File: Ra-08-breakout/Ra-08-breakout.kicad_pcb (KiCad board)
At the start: 2 copper layers, 3 parts, among them J1 Conn_01x09_Pin, J2 Conn_01x09_Pin, U1 RA-08H(915)

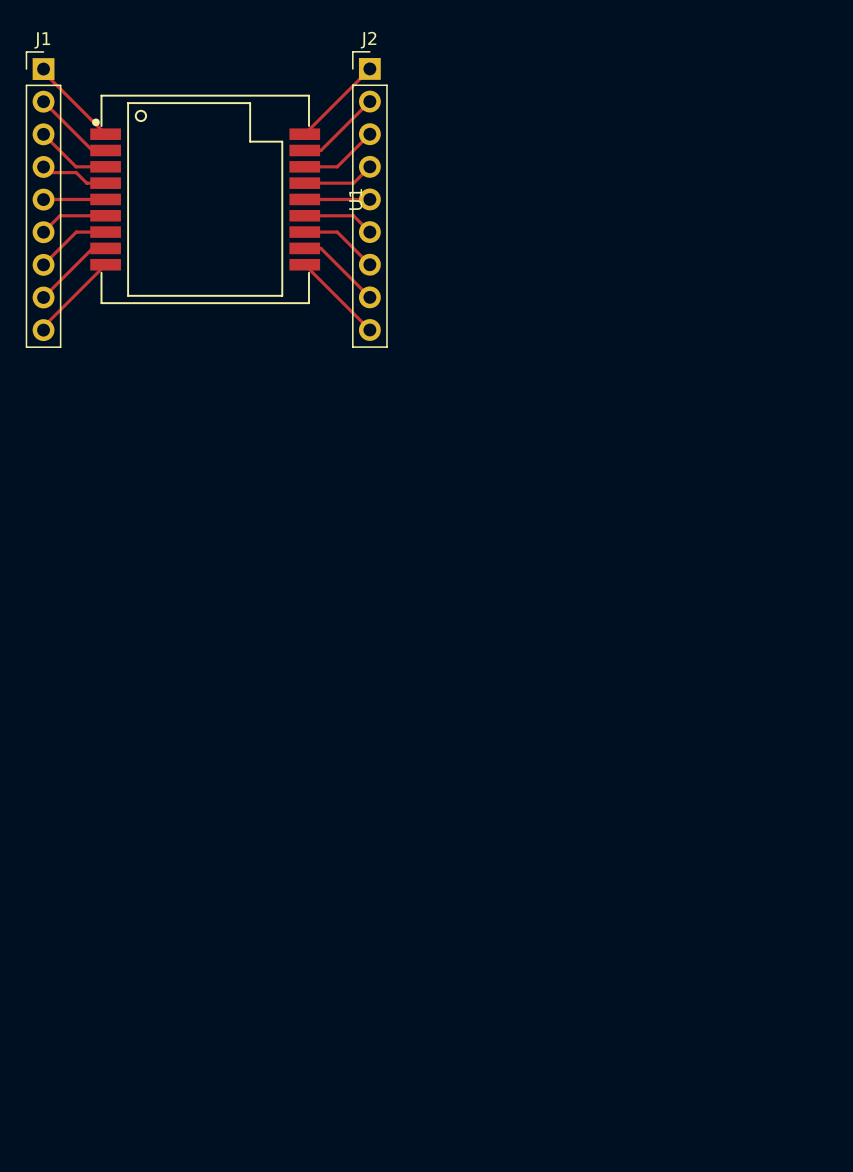
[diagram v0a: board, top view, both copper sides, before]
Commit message: Added Silkscreen
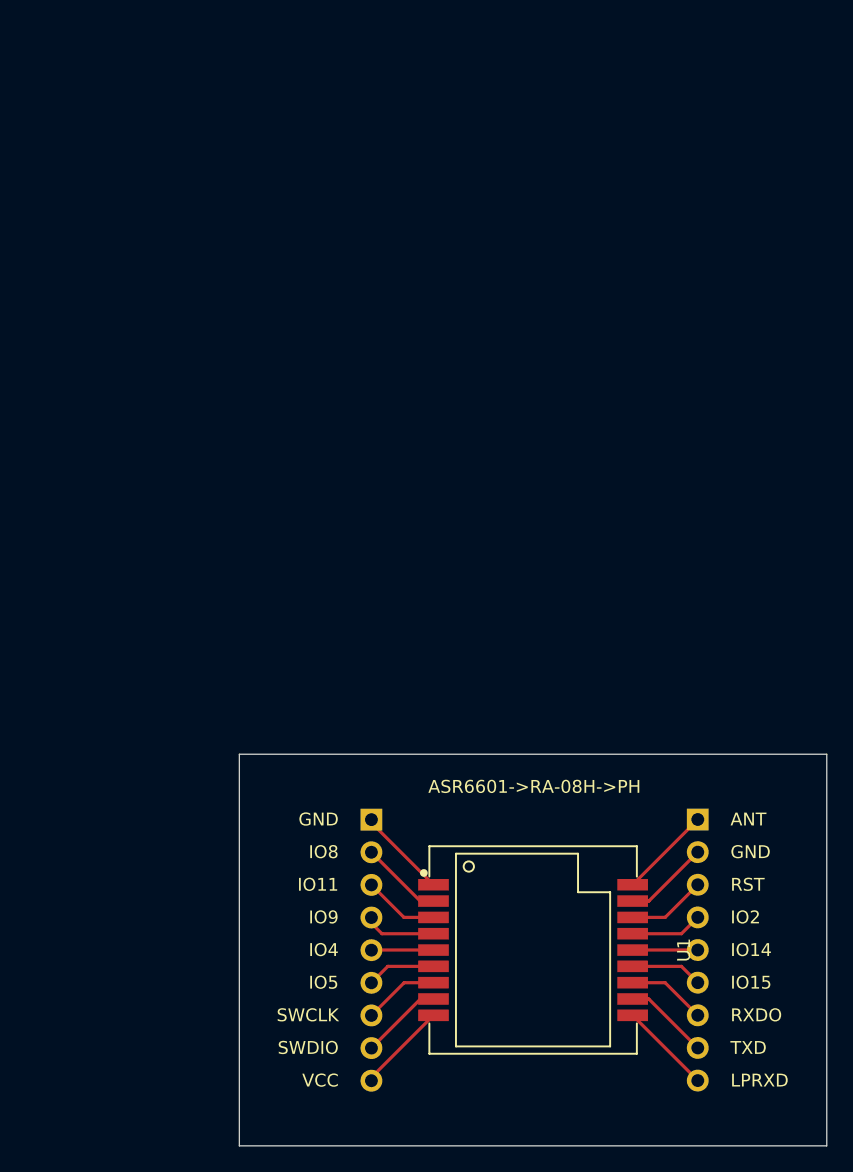
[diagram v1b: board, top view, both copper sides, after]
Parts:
- J1, J2: moved to B.Cu
- moved J1 63.8 mm to (147.4, 104.2), turned to 180 degrees
- moved J2 63.8 mm to (172.8, 104.1), turned to 180 degrees
- moved U1 63.8 mm to (160.0, 114.3)
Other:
- board outline added: 45.7 x 30.5 mm
- board text added: "ANT"
- board text added: "ASR6601->RA-08H->PH"
- board text added: "GND"
- board text added: "IO11"
- board text added: "IO14"
- board text added: "IO15"
- board text added: "IO2"
- board text added: "IO4"
- board text added: "IO5"
- board text added: "IO8"
- board text added: "IO9"
- board text added: "LPRXD"
- board text added: "RST"
- board text added: "RXDO"
- board text added: "SWCLK"
- board text added: "SWDIO"
- board text added: "TXD"
- board text added: "VCC"
